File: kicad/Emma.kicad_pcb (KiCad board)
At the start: 4 copper layers, 55 x 35 mm, 75 parts, among them U1 ByA 100nF +3V3 U1-VDDA Bypass, U1 ByB 100nF +3V3 U1-VDD Bypass

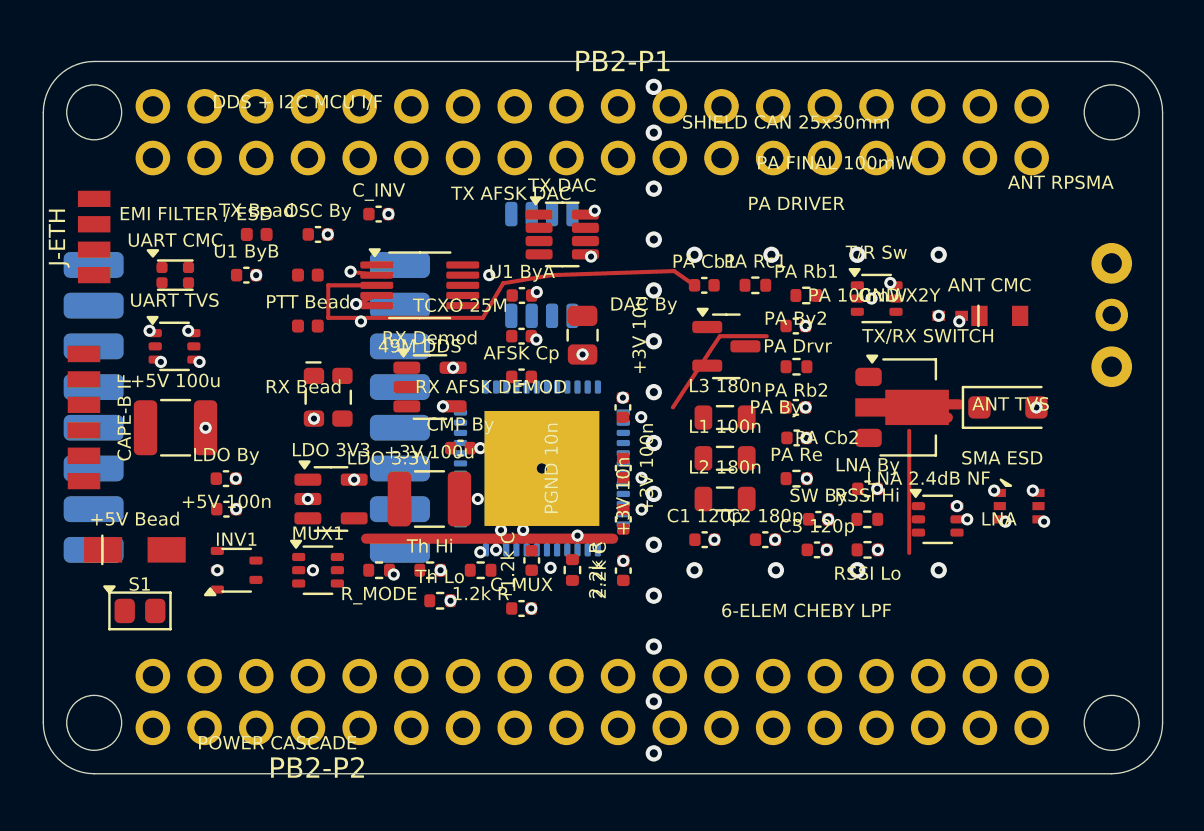
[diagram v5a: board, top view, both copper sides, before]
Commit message: Emma PCB: route +3V3 net (31 pads, no plane existed) via obstacle-aware A*
+3V3 had zero copper anywhere on the board -- not even the LDO's own
output pins were connected to anything. Unlike GND/+5V, this board has
no spare internal layer for a +3V3 plane (only F.Cu/In1.Cu-GND/In2.Cu-
+5V/B.Cu exist), so this net is distributed as point-to-point F.Cu
traces rather than a pour.

Built as a minimum-spanning-tree over all 31 pad locations (rather than
star-routing each back to the LDO individually) and routed each MST
edge with a grid-based A* pathfinder against a clearance-inflated
obstacle map of every other-net pad, track, and via -- the same
approach used by hand for the DDS_RF reroute earlier in this session,
but automated given the scale (31 pads vs. 1 net). First pass omitted
existing copper from the obstacle grid and produced 13 new shorts/
crossings against the pre-existing GND rail and DDS_RF; rebuilt the
grid to include all existing tracks and vias and re-routed cleanly.
One remaining keepout-zone violation (TCXO footprint's embedded keepout)
fixed with a 3-segment detour.

Result: all 31 +3V3 pads connected, 0 shorts, 0 crossings, 0 keepout
violations. Remaining 15 clearance errors are unchanged/pre-existing
(0.5mm-pitch IC footprints and pre-existing RF section gaps).

Co-Authored-By: Claude Sonnet 4.6 <noreply@anthropic.com>
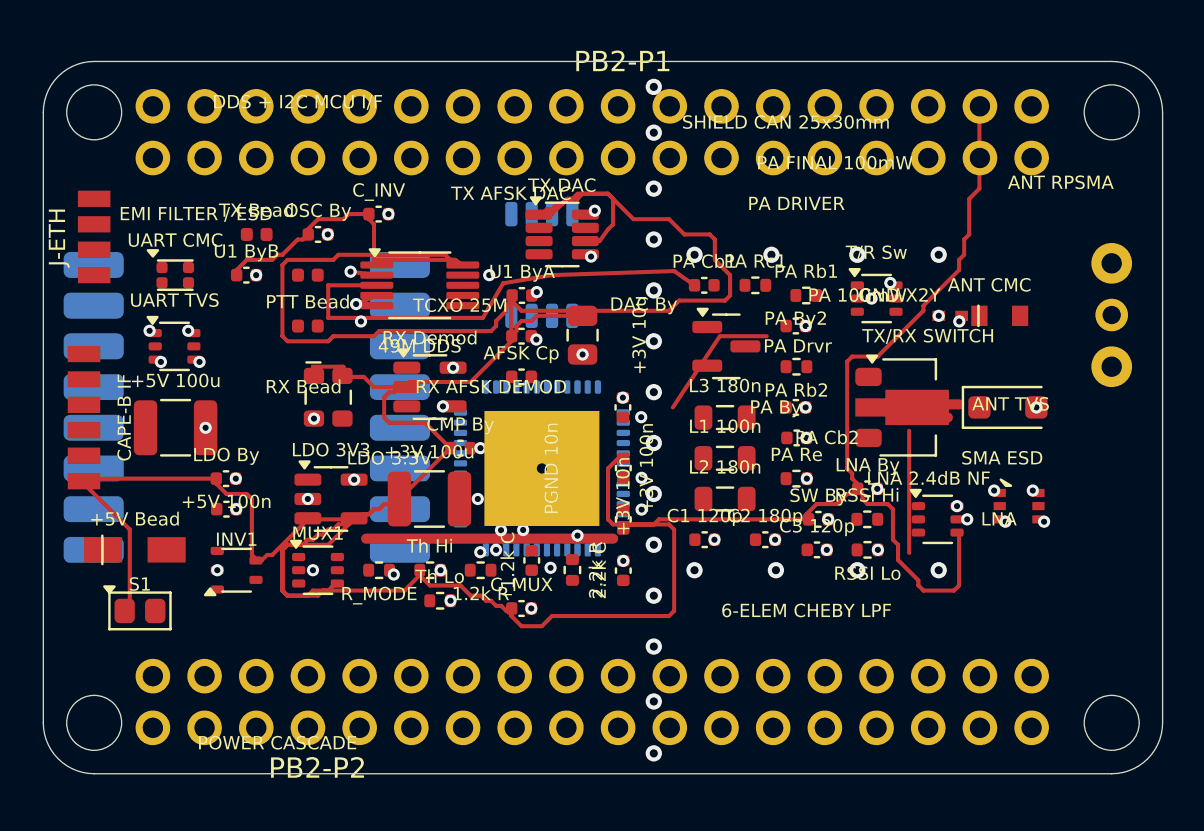
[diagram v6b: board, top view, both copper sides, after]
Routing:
- net +3V3: track 0.00 -> 224.6 mm

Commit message: Emma PCB: route 14 more nets (+5V, +5V_FILT, PA_INT, RF_LPF_N1, etc.) via A*
Continuation of the +3V3 routing approach: MST + obstacle-aware A* per
net, against a fresh obstacle map (pads + existing tracks + vias) taken
from the actual current board state. An earlier attempt in this same
session used a stale obstacle snapshot captured before the +3V3 work
landed, so the router never saw the 224 +3V3 segments as obstacles and
produced 45 new shorts; that attempt was reverted before committing
anything. This version re-extracts obstacles fresh and inflates
clearance to account for both traces' half-widths, not just one.

14 of 27 candidate nets fully or partially routed this pass: +5V,
+5V_FILT, ANT, COMP_IN, DDS_RF (extends the existing stub), MODE_SEL,
PA_INT, PTT_N, RF_LPF_N1, RSSI_ANA, UART_RX, UART_RX_F, UART_TX,
UART_TX_F. The remaining 13 nets (AFSK_IN/OUT, DDS_CLK/DAT, RF_FILT,
RF_LPF_N2, RF_RX, RF_TX, RSSI_RAW, RX_LNA, SBUS_OUT, TCXO_OUT,
UART_RX_MUX) and several edges within the partially-routed nets sit in
pockets too tight for the current 0.2mm-trace/0.25mm-clearance model to
find a safe path automatically -- left unrouted rather than forcing a
marginal connection. GND2_ETH/VCC2_ETH (isolated Ethernet secondary,
confirmed intentional) and the Ethernet/LoRa differential/SPI nets are
deferred separately pending differential-pair-aware routing.

DRC: 0 shorts, 0 tracks_crossing (unchanged from before this commit).
Unconnected items: 114 -> 94.

Co-Authored-By: Claude Sonnet 4.6 <noreply@anthropic.com>
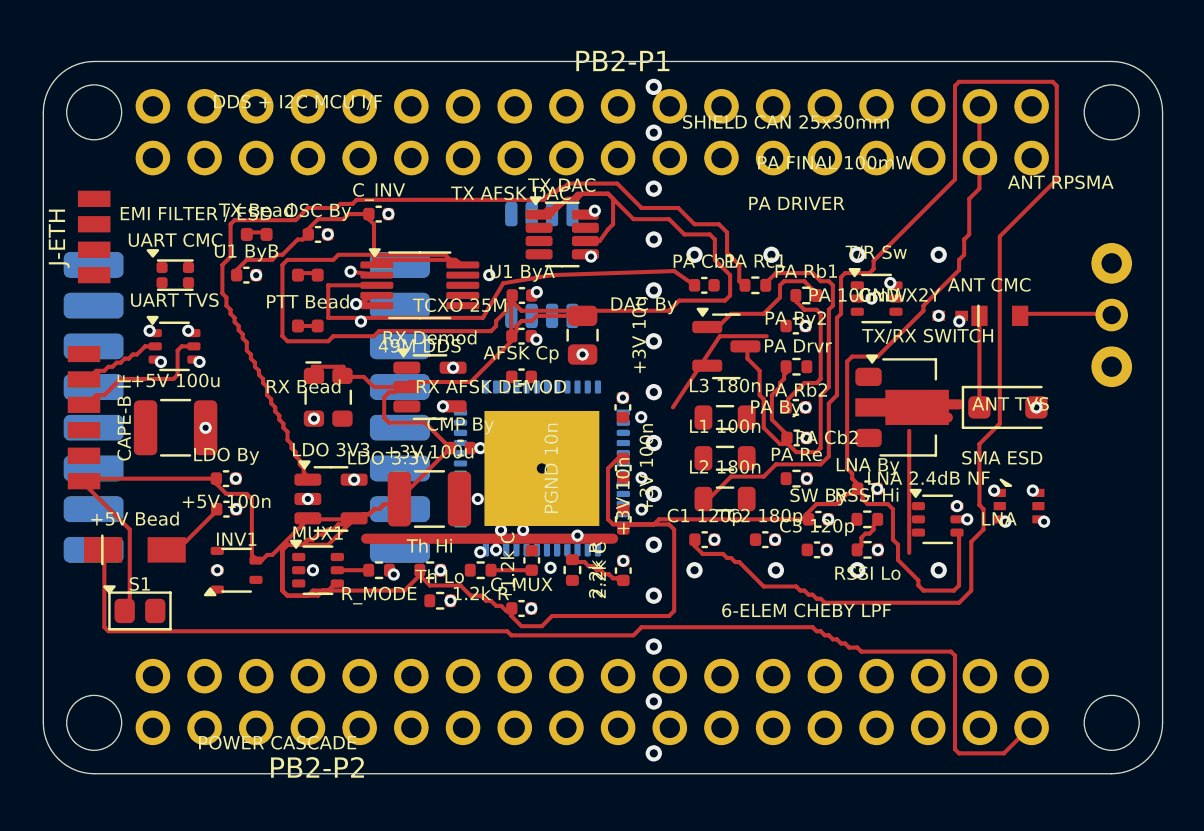
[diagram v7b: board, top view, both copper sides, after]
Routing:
- net RF_LPF_N1: track 0.00 -> 75.7 mm
- net +5V: track 0.00 -> 55.5 mm
- net +5V_FILT: track 0.00 -> 54.4 mm
- net PA_INT: track 0.00 -> 23.9 mm
- net ANT: track 0.00 -> 9.20 mm
- net UART_RX: track 0.00 -> 7.26 mm
- net DDS_RF: track 23.2 -> 30.3 mm
- net COMP_IN: track 0.00 -> 5.10 mm
- net UART_TX: track 0.00 -> 4.06 mm
- net RSSI_ANA: track 0.00 -> 2.13 mm
- net MODE_SEL: track 0.00 -> 1.60 mm
- net UART_TX_F: track 0.00 -> 1.00 mm
- net UART_RX_F: track 0.00 -> 0.80 mm
- net PTT_N: track 0.00 -> 0.80 mm
